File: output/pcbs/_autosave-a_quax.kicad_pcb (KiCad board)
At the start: 2 copper layers, 101.8 x 95.1 mm, 37 parts

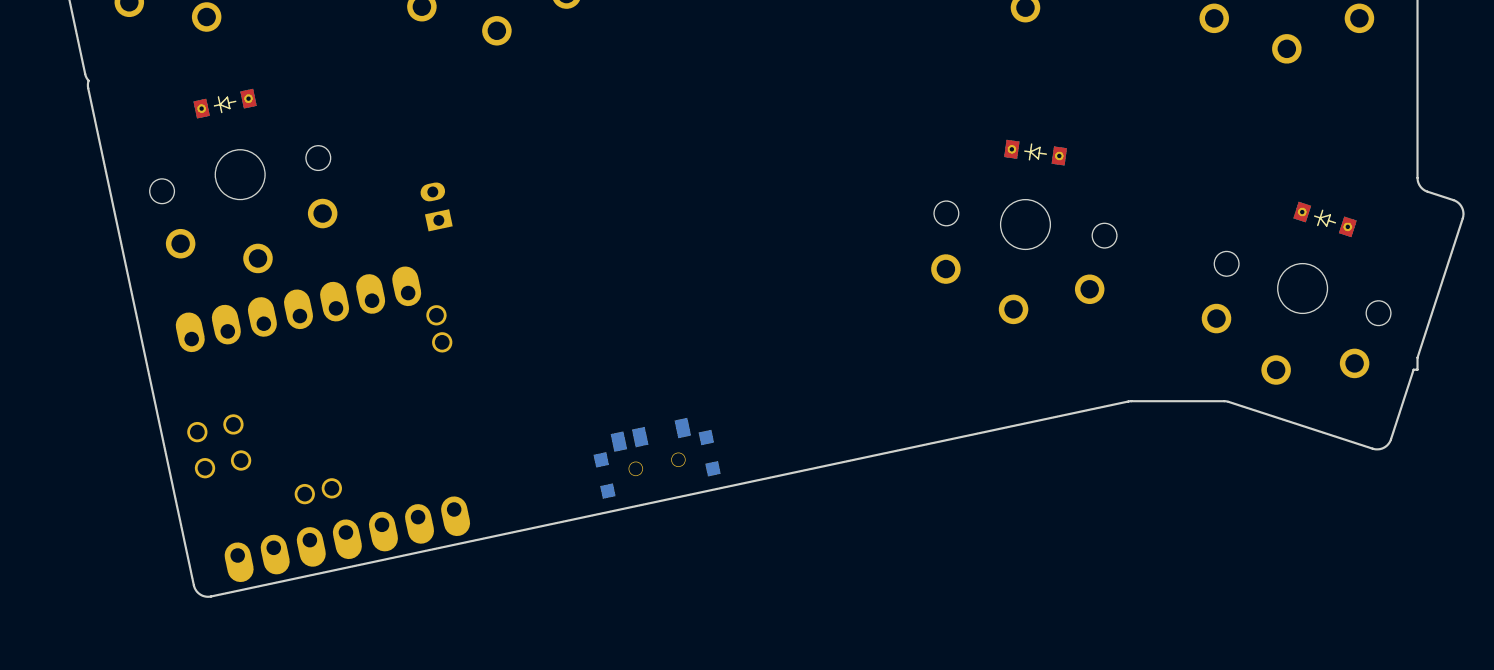
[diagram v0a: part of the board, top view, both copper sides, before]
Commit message: experimental mcu placement
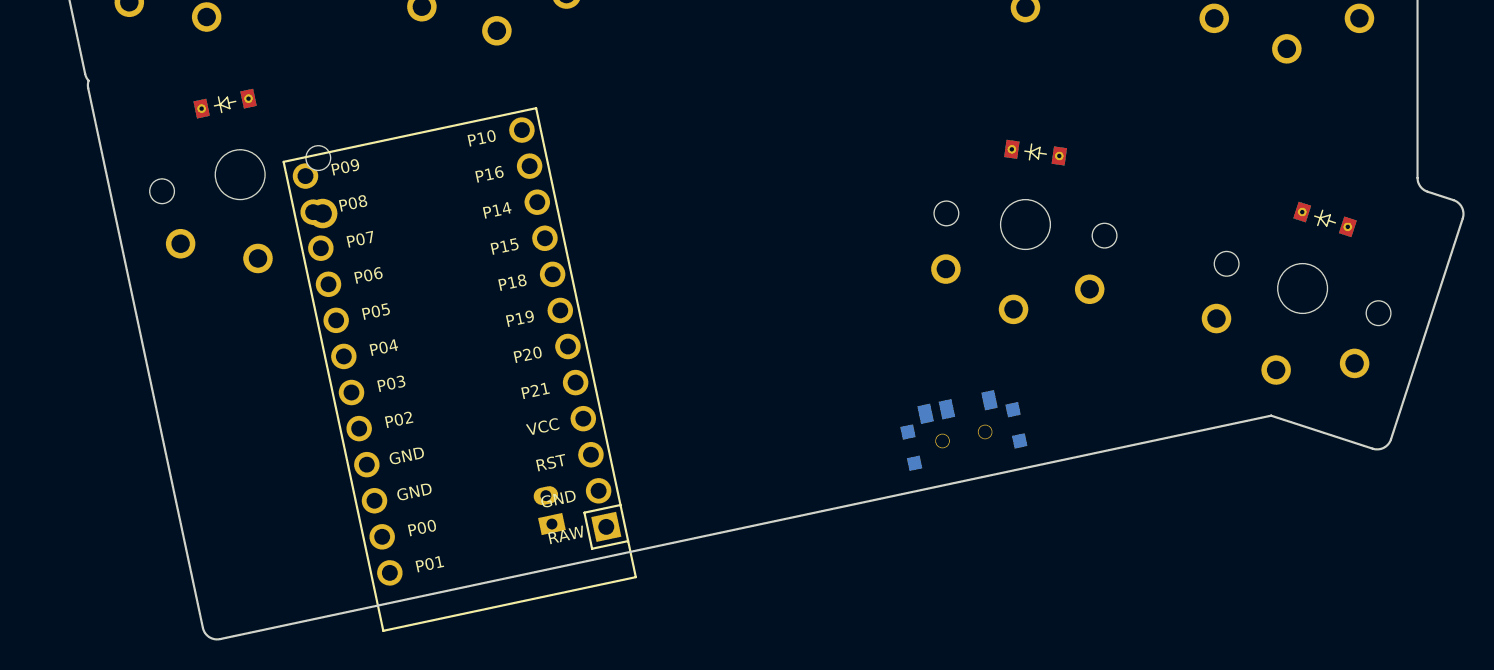
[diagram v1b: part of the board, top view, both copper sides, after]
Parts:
- D1, D10, D11, D12, D13, D14, D15, D16, D17, D2, D3, D4, D5, D6, D7, D8, D9: footprint ComboDiode -> diode
- MCU1: footprint xiao-ble-tht -> ProMicro
- moved JST1 22.3 mm to (35.7, 23.5)
- moved T1 21.2 mm to (64.3, 18.4)
- moved MCU1 10.4 mm to (29.3, 12.5)
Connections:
- net CLK renamed P18
- net NFC0 renamed P14
- net NFC1 renamed P16
- MCU1 pad 1: VCC5 -> RAW
- MCU1 pad 12: P6 -> P10
- MCU1 pad 13: P5 -> P1
- MCU1 pad 14: P4 -> P0
- MCU1 pad 15: P3 -> GND
- MCU1 pad 16: P2 -> GND
- MCU1 pad 17: P1 -> P2
- MCU1 pad 18: P0 -> P3
- MCU1 pad 19: DIO -> P4
- MCU1 pad 20: RST -> P5
- MCU1 pad 21: RAW -> P6
- MCU1 pad 22: GND -> P7
- MCU1 pad 3: VCC3 -> RST
- MCU1 pad 4: P10 -> VCC
- MCU1 pad 5: P9 -> P21
- MCU1 pad 6: P8 -> P20
- MCU1 pad 7: P7 -> P19
- MCU1 pad 9: GND -> P15
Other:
- board size 101.8 x 95.1 mm -> 101.8 x 98.1 mm
